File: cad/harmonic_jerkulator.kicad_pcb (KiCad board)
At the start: 2 copper layers, 91 x 87 mm, 41 parts, among them J101 CONN_AUDIO_IN, J102 CONN_AUDIO_OUT, J103 CONN_PSU, J105 PNP, J106 NPN, J107 SW_BYPASS, J108 DIODE1, J109 SW_DIODE, J110 DIODE2, J111 CONN_CONN_BOARD, J112 SW_DIODE, J113 CONN_CIRCUIT_BOARD, K101 TQ2SA-5V, Q101 BC850, Q102 BC856, Q103 DTC123Y, Q104 DTC123Y, U101 4013

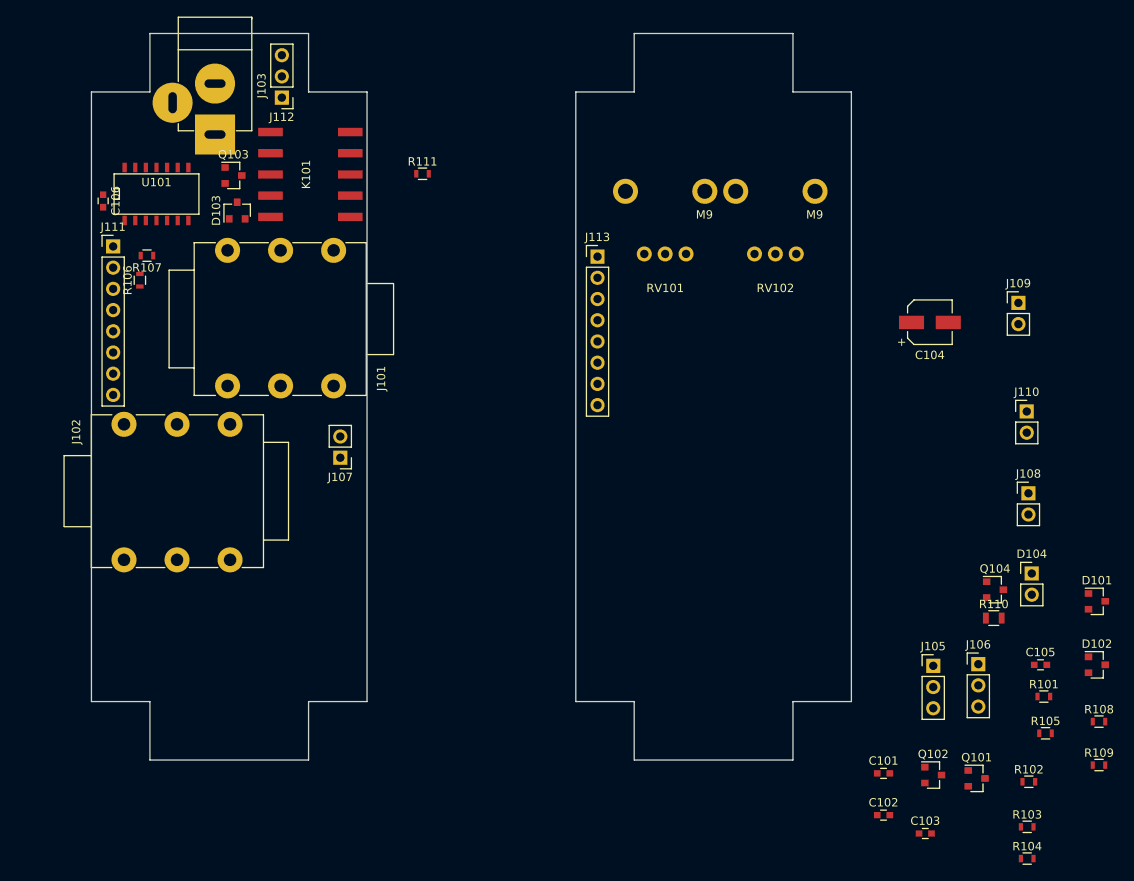
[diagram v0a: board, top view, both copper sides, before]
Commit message: Checked mechanics.
Components placed.
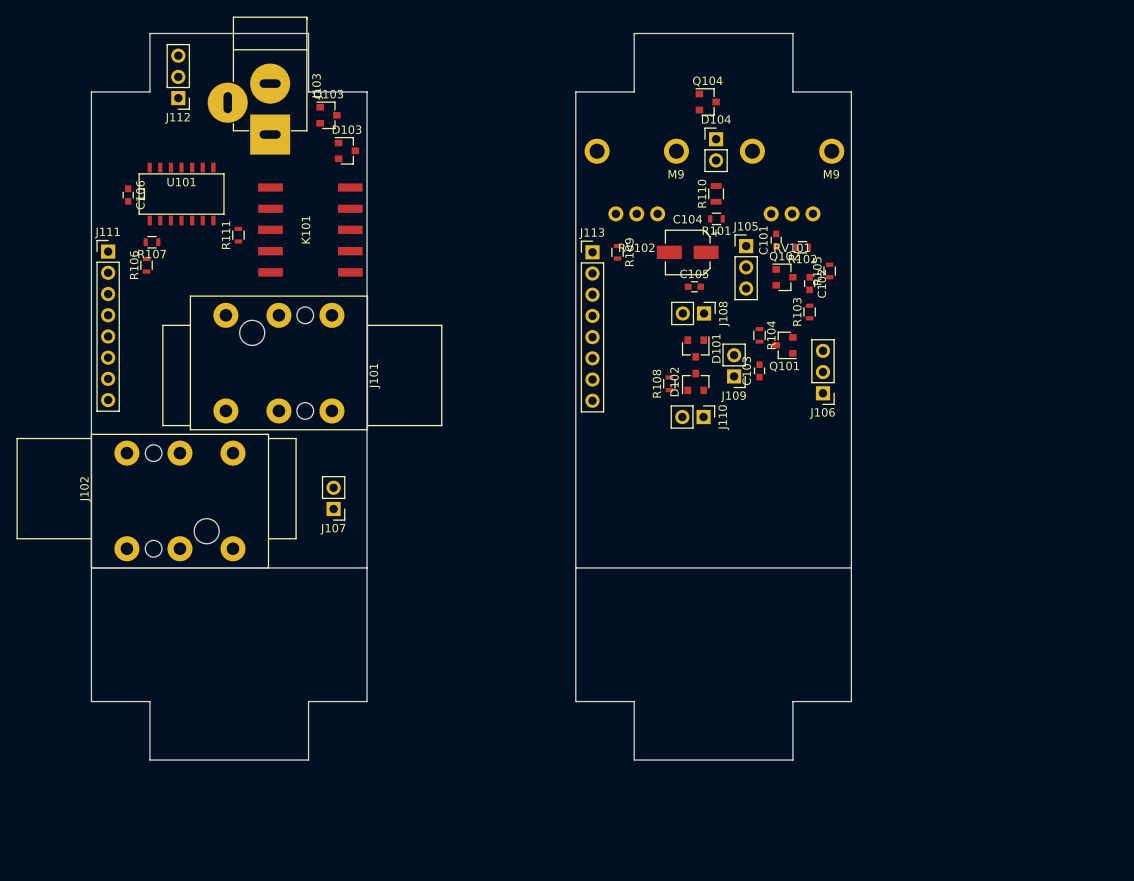
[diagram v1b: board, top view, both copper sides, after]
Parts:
- J101: value CONN_AUDIO_IN -> JACK_IN; footprint Connect:NMJ6HCD2 -> flax_lib:CLIFF_FCR5005x
- J102: value CONN_AUDIO_OUT -> JACK_OUT; footprint Connect:NMJ6HCD2 -> flax_lib:CLIFF_FCR5005x
- moved R109 84.2 mm to (127.0, 72.2), turned to 270 degrees
- moved R104 70.4 mm to (144.0, 82.2), turned to 270 degrees
- moved R102 69.5 mm to (149.2, 71.6), turned to 180 degrees
- moved R101 69.3 mm to (138.8, 68.2), turned to 180 degrees
- moved Q104 67.8 mm to (137.8, 54.2)
- moved R103 66.9 mm to (150.0, 79.3), turned to 90 degrees
- moved R108 65.4 mm to (133.2, 88.0), turned to 90 degrees
- moved C101 65.1 mm to (146.0, 70.8), turned to 90 degrees
- moved D104 64.3 mm to (138.8, 58.7)
- moved C102 64.3 mm to (150.0, 76.0), turned to 270 degrees
- moved Q102 62.2 mm to (147.0, 75.2)
- moved C105 61.4 mm to (136.2, 76.3)
- moved R105 61.1 mm to (152.4, 74.5), turned to 90 degrees
- moved R110 60.7 mm to (138.8, 65.2), turned to 90 degrees
- moved C103 58.8 mm to (144.0, 86.4), turned to 90 degrees
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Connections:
- J101 pad 2: /AUDIO_IN -> (no net)
- J101 pad 3: (no net) -> /AUDIO_IN
- J101 pad 4: (no net) -> VSS
- J102 pad 2: /AUDIO_OUT -> (no net)
- J102 pad 3: (no net) -> /AUDIO_OUT
- J102 pad 4: (no net) -> VSS
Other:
- outline, holes or cut-outs redrawn

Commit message: Corrected schematic : serial resistors on relay coil. Started layout.
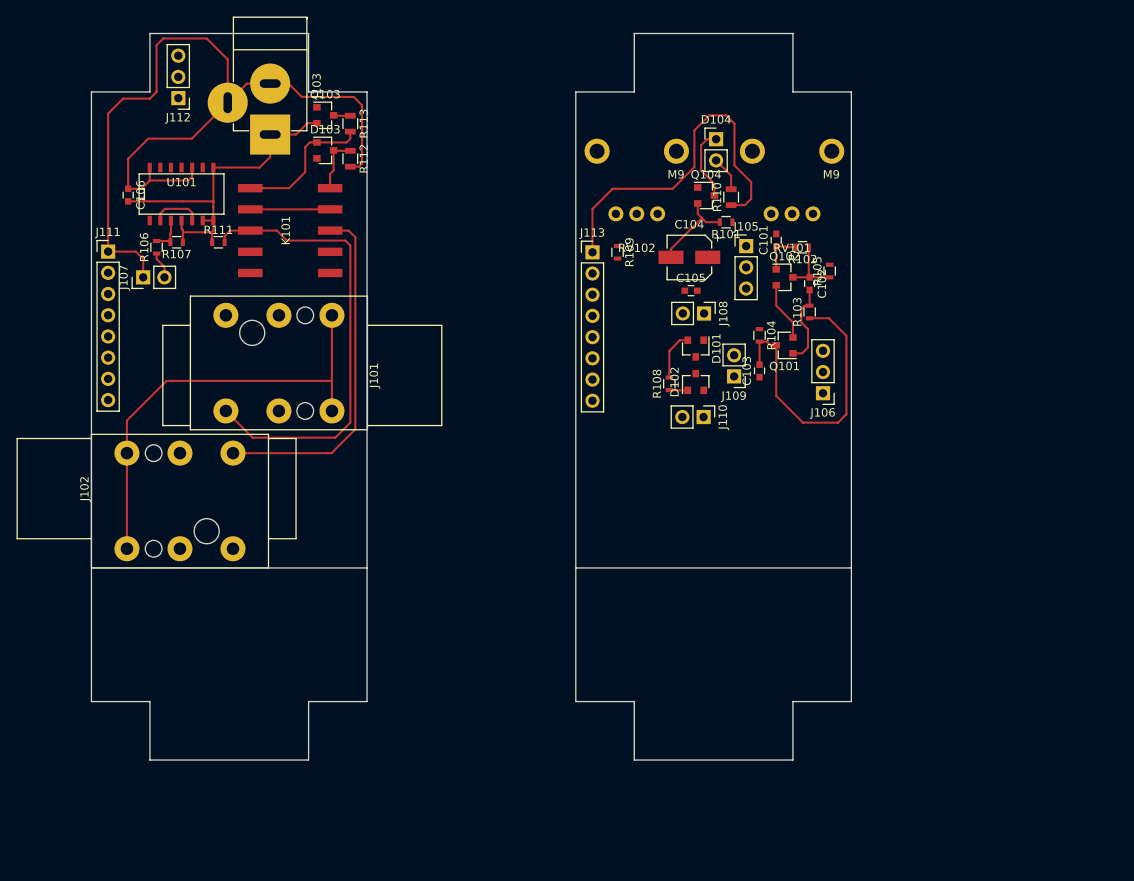
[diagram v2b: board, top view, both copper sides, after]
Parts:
- added R112: 150, Resistors_SMD:R_0805, F.Cu at (95.0, 61.0)
- added R113: 150, Resistors_SMD:R_0805, F.Cu at (95.0, 56.8)
- moved J107 35.9 mm to (70.2, 75.2), turned to 90 degrees
- moved Q104 11.2 mm to (137.6, 65.4)
- moved R107 2.95 mm to (74.2, 71.0)
- moved D103 2.60 mm to (92.0, 60.0)
- moved R111 2.55 mm to (79.2, 71.0), turned to 0 degrees
- moved R106 2.46 mm to (71.8, 71.6)
- moved K101 2.42 mm to (87.8, 69.6)
- moved R110 1.84 mm to (140.6, 65.6)
- moved R101 1.22 mm to (140.0, 68.6)
- moved C104 0.63 mm to (135.6, 72.8)
- moved C105 0.62 mm to (135.8, 76.8)
- moved Q103 0.40 mm to (92.0, 55.8)
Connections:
- D103 pad 3: +BATT -> Net-(D103-Pad3)
- J103 pad 3: +BATT -> VDD
- J111 pad 2: GND -> /BYPASS_CMD
- J111 pad 3: /FX_IN_A -> GND
- J111 pad 5: /FX_OUT_A -> /SW_DIODE_2A
- J111 pad 6: /SW_DIODE_2A -> /FX_IN_A
- J111 pad 7: GND -> /FX_OUT_A
- J111 pad 8: /BYPASS_CMD -> GND
- J113 pad 2: GNDD -> /LED_CMD_B
- J113 pad 3: /FX_IN_B -> GNDD
- J113 pad 5: /FX_OUT_B -> /SW_DIODE_2B
- J113 pad 6: /SW_DIODE_2B -> /FX_IN_B
- J113 pad 7: GNDD -> /FX_OUT_B
- J113 pad 8: /LED_CMD_B -> GNDD
- K101 pad 1: +BATT -> Net-(D103-Pad3)
- Q103 pad 3: Net-(D103-Pad1) -> Net-(Q103-Pad3)
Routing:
- net VDD: track 0.00 -> 106.7 mm
- net VSS: track 0.00 -> 96.2 mm
- net /AUDIO_IN: track 0.00 -> 55.0 mm
- net VAA: track 0.00 -> 42.4 mm
- net /AUDIO_OUT: track 0.00 -> 42.2 mm
- net Net-(C103-Pad2): track 0.00 -> 35.8 mm
- net Net-(D103-Pad1): track 0.00 -> 17.0 mm
- net GNDD: track 0.00 -> 16.5 mm
- net Net-(C102-Pad2): track 0.00 -> 10.1 mm
- net Net-(K101-Pad2): track 0.00 -> 9.56 mm
- net Net-(D104-Pad1): track 0.00 -> 8.77 mm
- net Net-(C102-Pad1): track 0.00 -> 8.04 mm
- net Net-(C104-Pad1): track 0.00 -> 7.08 mm
- net Net-(D103-Pad3): track 0.00 -> 6.71 mm
- net Net-(U101-Pad2): track 0.00 -> 6.02 mm
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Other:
- net class Default: clearance 0.2 -> 0.25; via_dia 0.6 -> 1.5; via_drill 0.4 -> 0.8
- rule trace_clearance: 0.2 -> 0.25

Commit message: Corrected pots polarity.
Connected GND and VSS.
Done single-side layout on Connectors board.
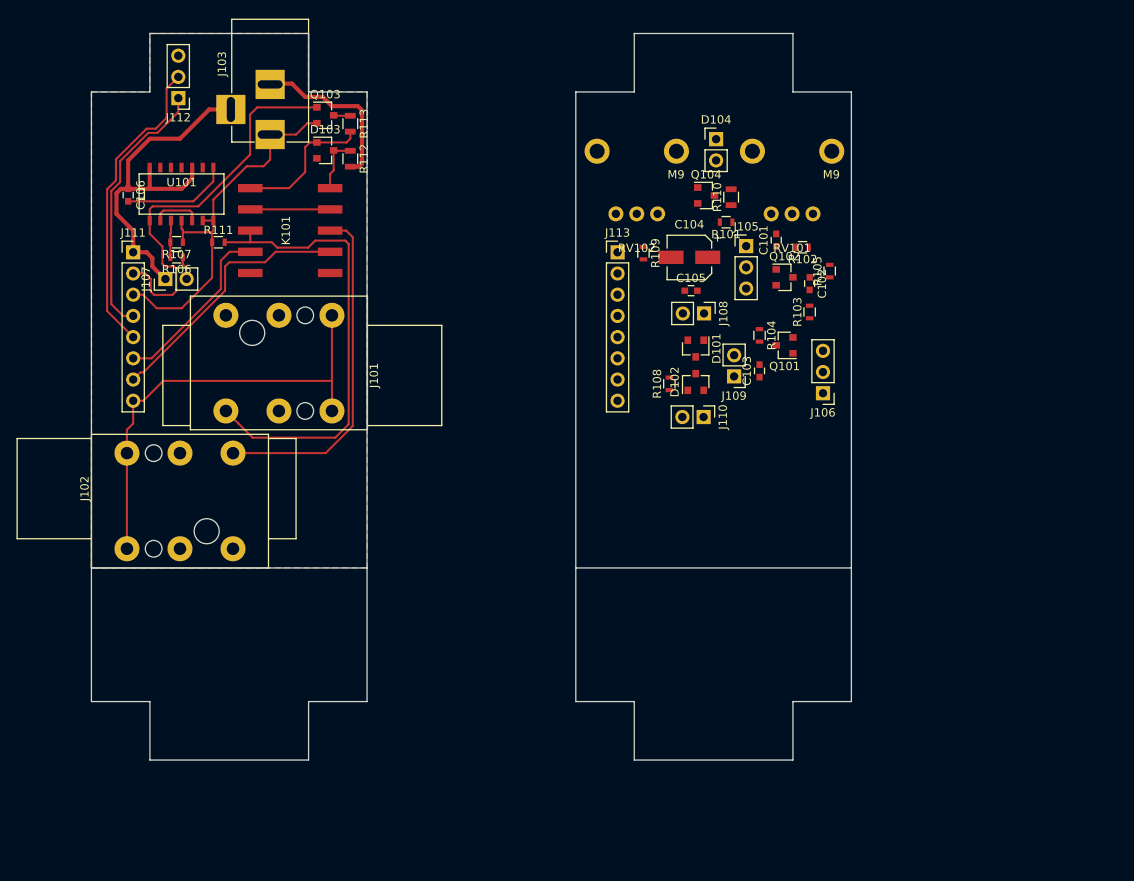
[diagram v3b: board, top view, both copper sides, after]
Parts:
- J103: footprint Connect:JACK_ALIM -> Connect:BARREL_JACK
- moved R109 3.10 mm to (130.1, 72.3)
- moved J111 3.00 mm to (69.0, 72.2)
- moved J113 3.00 mm to (127.0, 72.2)
- moved R106 2.68 mm to (74.2, 72.8), turned to 180 degrees
- moved J107 2.67 mm to (72.9, 75.4)
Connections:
- C106 pad 2: VSS -> GND
- J101 pad 1: VSS -> GND
- J101 pad 4: VSS -> GND
- J102 pad 1: VSS -> GND
- J102 pad 4: VSS -> GND
- J103 pad 1: VSS -> GND
- Q103 pad 2: VSS -> GND
- R107 pad 1: VSS -> GND
- R111 pad 1: VSS -> GND
- RV101 pad 1: /FX_IN_B -> Net-(R101-Pad1)
- RV101 pad 3: Net-(R101-Pad1) -> /FX_IN_B
- RV102 pad 1: Net-(R109-Pad1) -> GNDD
- RV102 pad 3: GNDD -> Net-(R109-Pad1)
- U101 pad 4: VSS -> GND
- U101 pad 6: VSS -> GND
- U101 pad 7: VSS -> GND
- U101 pad 8: VSS -> GND
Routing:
- net GND: track 0.00 -> 113.5 mm
- net VSS: track 96.2 -> 0.00 mm
- net /BYPASS_CMD: track 0.00 -> 47.0 mm
- net VAA: track 42.4 -> 0.00 mm
- net VDD: track 106.7 -> 65.8 mm
- net /SW_DIODE_2A: track 0.00 -> 36.6 mm
- net Net-(C103-Pad2): track 35.8 -> 0.00 mm
- net /SW_DIODE_1A: track 0.00 -> 31.8 mm
- net /FX_OUT_A: track 0.64 -> 31.6 mm
- net /FX_IN_A: track 0.00 -> 21.3 mm
- net GNDD: track 16.5 -> 0.00 mm
- net Net-(C102-Pad2): track 10.1 -> 0.00 mm
- net Net-(D104-Pad1): track 8.77 -> 0.00 mm
- net Net-(C102-Pad1): track 8.04 -> 0.00 mm
- net Net-(C104-Pad1): track 7.08 -> 0.00 mm
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- added copper zone on F.Cu, net GND
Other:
- net class vaa added: clearance 0.25, trace_width 0.5, via_dia 1.5, via_drill 0.8
- net class vdd added: clearance 0.25, trace_width 0.5, via_dia 1.5, via_drill 0.8

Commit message: Finished layout.
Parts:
- moved R105 3.74 mm to (151.6, 70.8)
- moved R101 2.80 mm to (137.2, 68.6)
- moved J106 2.51 mm to (150.2, 87.0)
- moved C102 2.37 mm to (151.6, 74.2)
- moved R104 2.37 mm to (142.4, 80.4)
- moved Q101 2.03 mm to (145.0, 83.0)
- moved Q102 1.84 mm to (148.8, 74.8)
- moved C105 1.02 mm to (134.8, 76.6)
- moved Q103 1.00 mm to (92.0, 56.8)
- moved R103 0.96 mm to (150.6, 78.6), turned to 180 degrees
- moved D103 0.60 mm to (92.0, 60.6)
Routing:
- net GNDD: track 0.00 -> 130.9 mm, vias 0 -> 3
- net (no net): track 0.00 -> 83.5 mm
- net /SW_DIODE_2B: track 0.00 -> 75.7 mm, vias 0 -> 2
- net VAA: track 0.00 -> 70.5 mm, vias 0 -> 1
- net /FX_IN_B: track 0.00 -> 63.1 mm
- net /SW_DIODE_1B: track 0.00 -> 46.3 mm, vias 0 -> 2
- net Net-(C104-Pad1): track 0.00 -> 33.1 mm, vias 0 -> 2
- net /FX_OUT_B: track 0.00 -> 30.5 mm
- net Net-(C103-Pad2): track 0.00 -> 30.0 mm, vias 0 -> 1
- net /LED_CMD_B: track 0.00 -> 21.2 mm, vias 0 -> 1
- net Net-(C102-Pad1): track 0.00 -> 17.0 mm, vias 0 -> 1
- net Net-(D104-Pad2): track 0.00 -> 16.5 mm, vias 0 -> 1
- net Net-(D104-Pad1): track 0.00 -> 15.7 mm, vias 0 -> 1
- net Net-(C102-Pad2): track 0.00 -> 15.4 mm, vias 0 -> 1
- net Net-(C101-Pad1): track 0.00 -> 10.2 mm, vias 0 -> 1
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- added copper zone on B.Cu, net GNDD
- added copper zone on F.Cu, net GNDD
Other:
- board text added: "RANDAGODRON"
- board text added: "RANDAGODRON harmonic jerkulator v01"
- board text added: "harmonic"
- board text added: "jerkulator"
- board text added: "v01"

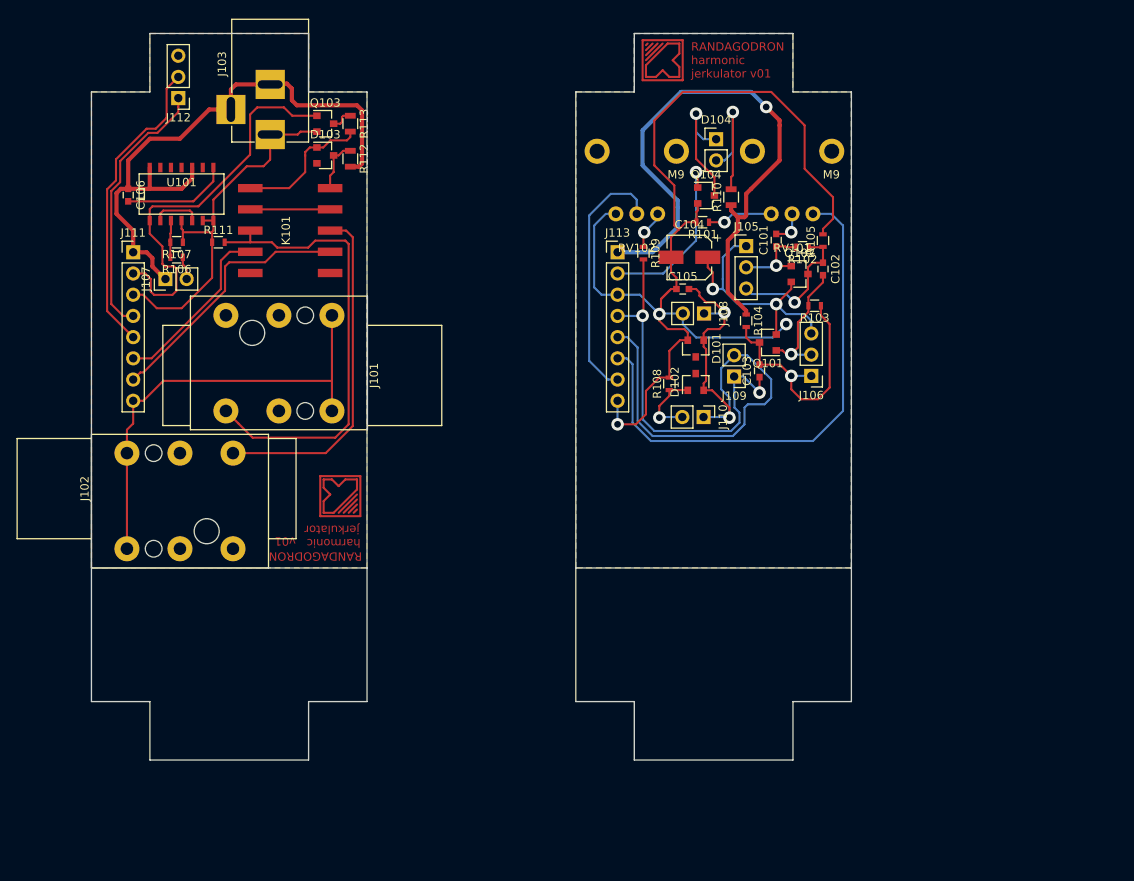
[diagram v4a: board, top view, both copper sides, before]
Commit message: Corrections on layout.
Exported layout.
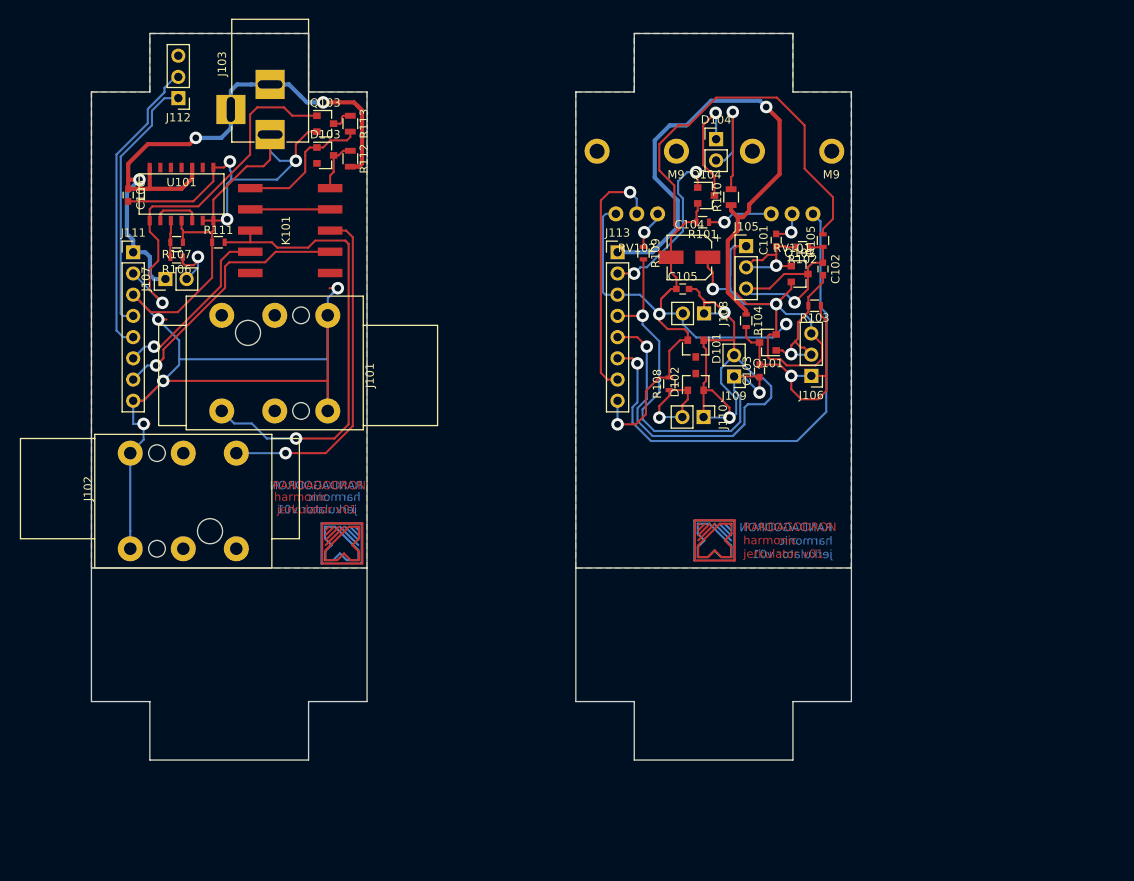
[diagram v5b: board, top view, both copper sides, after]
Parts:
- moved J101 0.50 mm to (96.5, 87.0)
- moved J102 0.40 mm to (64.4, 100.5)
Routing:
- net GND: track 113.1 -> 199.4 mm, vias 0 -> 7
- net (no net): track 83.5 -> 166.9 mm
- net Net-(C104-Pad1): track 33.1 -> 63.9 mm
- net /SW_DIODE_2B: track 75.7 -> 89.7 mm, vias 2 -> 3
- net Net-(C102-Pad1): track 17.0 -> 25.1 mm
- net /SW_DIODE_1B: track 46.3 -> 51.1 mm
- net Net-(C101-Pad1): track 10.2 -> 14.5 mm
- net GNDD: track 130.9 -> 126.7 mm
- net VAA: track 70.5 -> 66.7 mm
- net Net-(J107-Pad2): track 2.79 -> 6.52 mm, vias 0 -> 1
- net Net-(D102-Pad1): track 8.81 -> 12.3 mm
- net /FX_IN_B: track 63.1 -> 59.9 mm, vias 0 -> 1
- net VDD: track 74.0 -> 77.1 mm, vias 0 -> 3
- net Net-(C102-Pad2): track 15.4 -> 18.0 mm
- net Net-(C103-Pad2): track 30.0 -> 31.5 mm
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- added copper zone on B.Cu, net GND
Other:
- board text added: "jerkulator v01"
- board text removed: "jerkulator"
- board text removed: "v01"
